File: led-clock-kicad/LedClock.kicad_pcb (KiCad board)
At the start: 2 copper layers, 176.4 x 21.4 mm, 47 parts, among them J1 Barrel_Jack, J2 AVR-ISP-10, U1 ATmega32-16A, U2 STP16CPC05MTR, U3 STP16CPC05MTR, Y1 Crystal

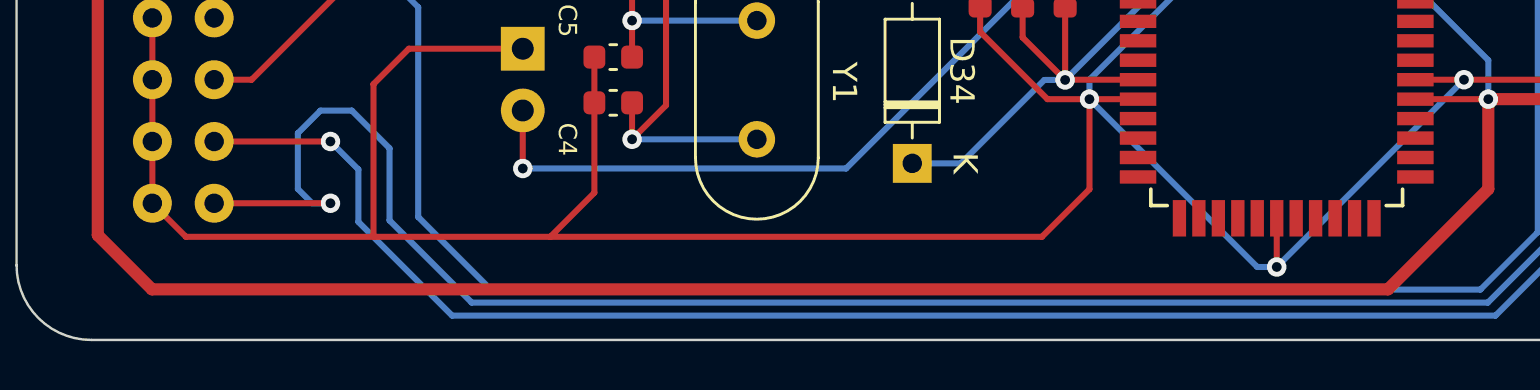
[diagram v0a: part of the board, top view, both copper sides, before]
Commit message: Connected AVCC to the 5 volts rail.
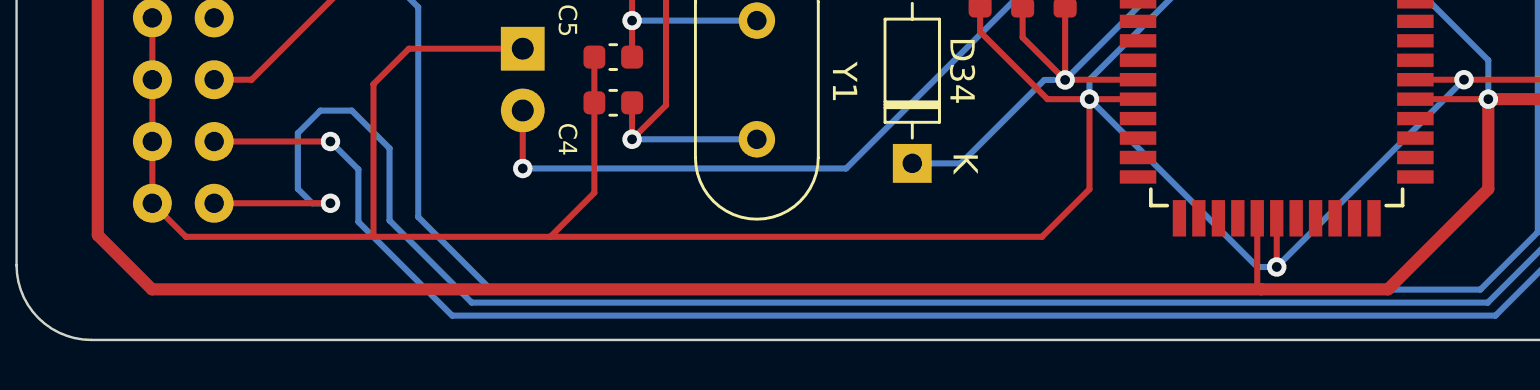
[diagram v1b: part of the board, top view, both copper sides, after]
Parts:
- R5, R6: value 7.15k -> 7.32k
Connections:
- net Net-(D33-A) renamed /PD2
- net Net-(D34-A) renamed /Reset
- net Net-(J2-MISO) renamed /PB6
- net Net-(J2-MOSI) renamed /PB5
- net Net-(J2-SCK) renamed /PB7
- net Net-(U1-PB4) renamed /PB4
- U1 pad 27: unconnected-(U1-AVCC-Pad27) -> +5V
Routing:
- net +5V: track 385.4 -> 388.2 mm
